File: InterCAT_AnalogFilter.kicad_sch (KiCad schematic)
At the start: 37 parts, among them T1 LM-NP-1001-B1L, T2 LM-NP-1001-B1L, T3 LM-NP-1001-B1L, T4 LM-NP-1001-B1L, U4 MCP6002, U5 MCP6002, U6 MCP6002

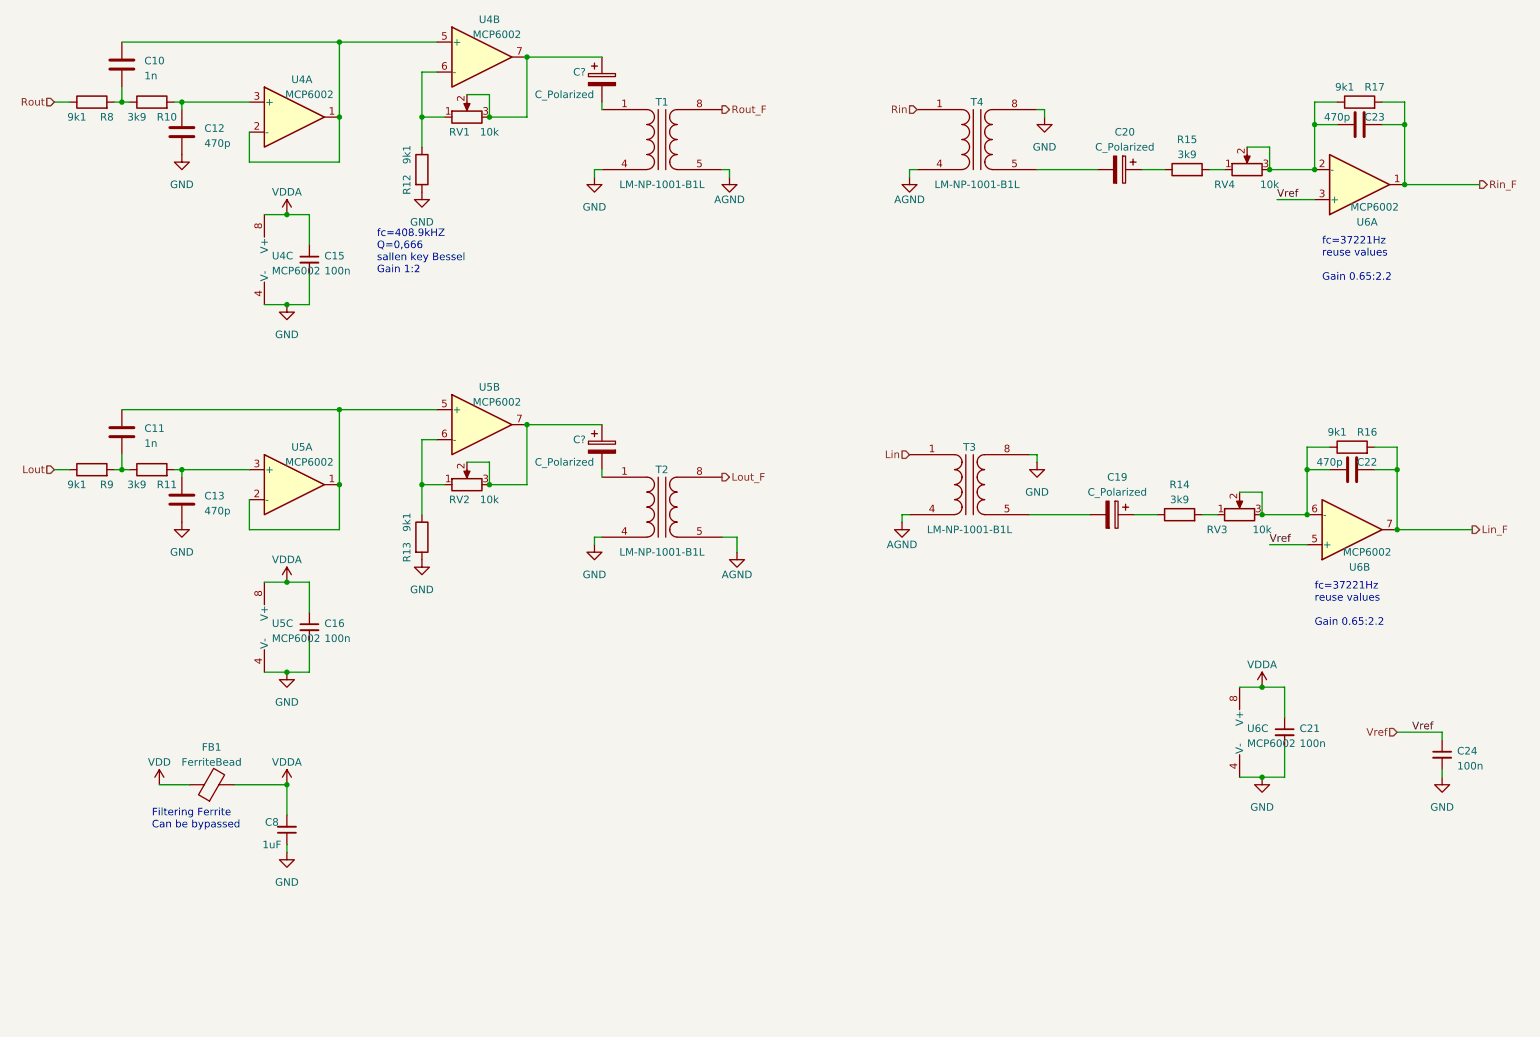
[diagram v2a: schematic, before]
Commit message: removed jack connectors, added testpoints on DAC
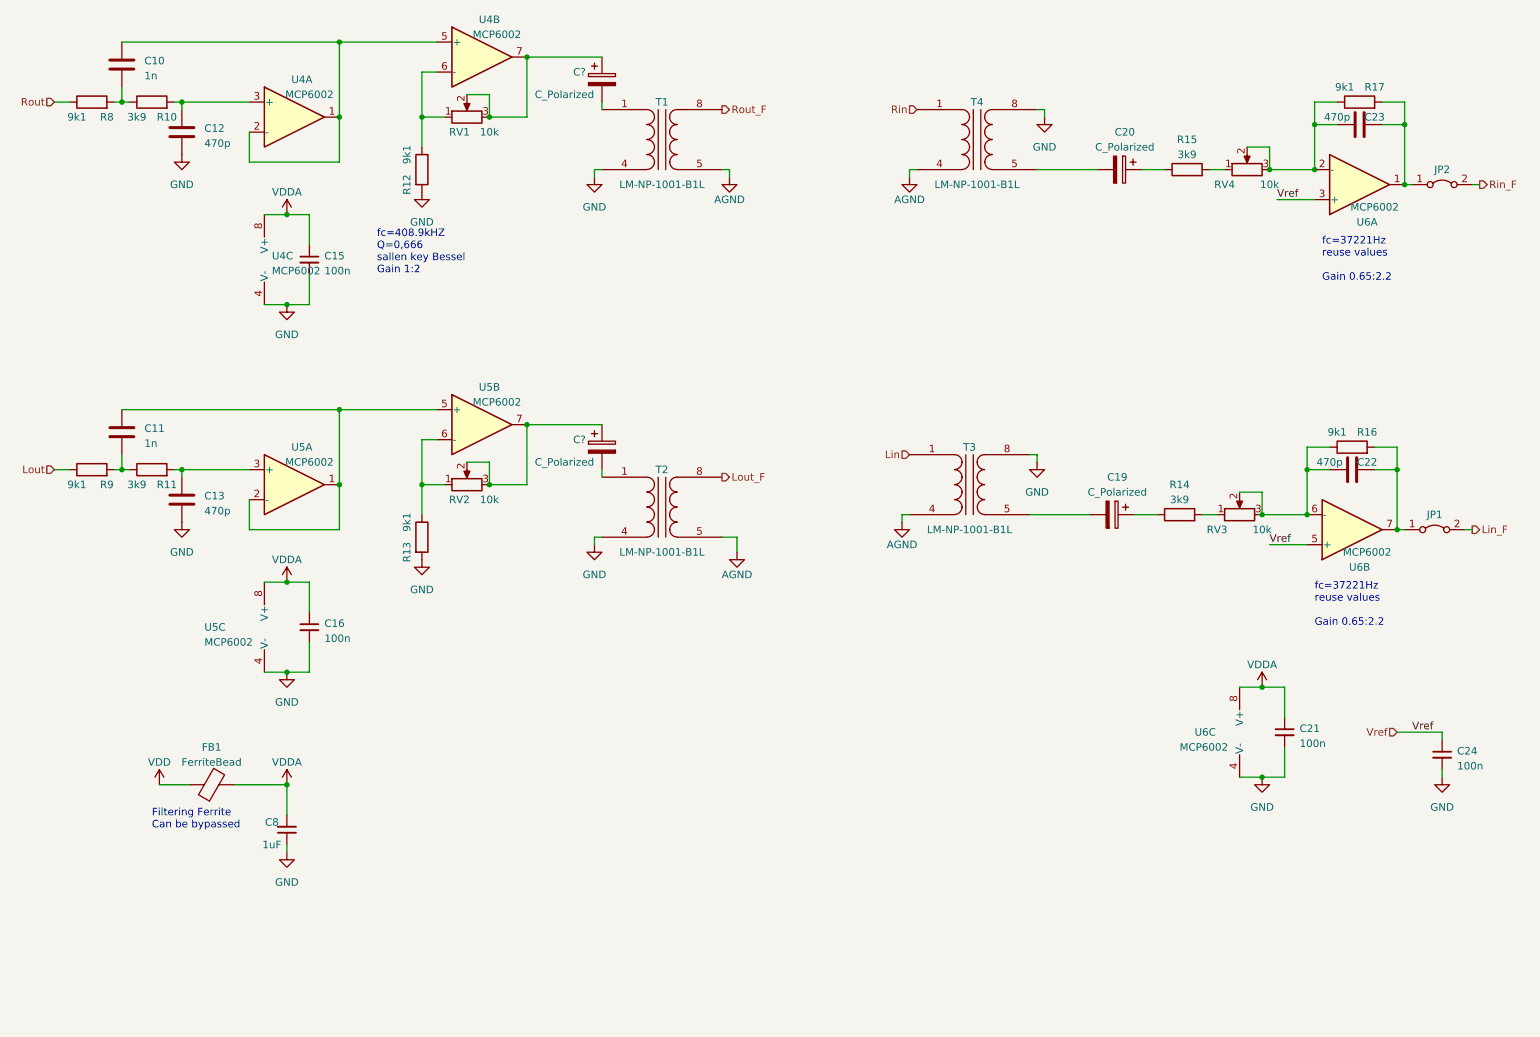
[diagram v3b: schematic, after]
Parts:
- added JP1, JP2: Jumper_2_Bridged, Jumper:SolderJumper-2_P1.3mm_Bridged_RoundedPad1.0x1.5mm, symbol Jumper:Jumper_2_Bridged
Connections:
- net Lin_F: now also JP1.2 (B); no longer C22.2, R16.2, U6.7
- net Rin_F: now also JP2.2 (B); no longer C23.2, R17.2, U6.1
- new net: C22.2, JP1.1 (A), R16.2, U6.7
- new net: C23.2, JP2.1 (A), R17.2, U6.1
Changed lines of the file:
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@@
   (junction (at 72.39 26.67) (diameter 0) (color 0 0 0 0)
   )
+  (junction (at 252.73 50.8) (diameter 0) (color 0 0 0 0)
+  )
   (junction (at 86.36 39.37) (diameter 0) (color 0 0 0 0)
   )
@@
   (junction (at 97.79 101.6) (diameter 0) (color 0 0 0 0)
   )
-  (junction (at 252.73 50.8) (diameter 0) (color 0 0 0 0)
-  )
   (junction (at 104.14 91.44) (diameter 0) (color 0 0 0 0)
   )
@@
   (junction (at 35.56 36.83) (diameter 0) (color 0 0 0 0)
   )
+  (junction (at 251.46 109.22) (diameter 0) (color 0 0 0 0)
+  )
   (junction (at 97.79 39.37) (diameter 0) (color 0 0 0 0)
   )
@@
   (junction (at 35.56 99.06) (diameter 0) (color 0 0 0 0)
   )
-  (junction (at 251.46 109.22) (diameter 0) (color 0 0 0 0)
-  )
   (junction (at 72.39 101.6) (diameter 0) (color 0 0 0 0)
   )
@@
     (stroke (width 0) (type default))
   )
+  (wire (pts (xy 264.16 50.8) (xy 265.43 50.8))
+    (stroke (width 0) (type default))
+  )
   (wire (pts (xy 236.22 99.06) (xy 240.03 99.06))
     (stroke (width 0) (type default))
@@
     (stroke (width 0) (type default))
   )
-  (wire (pts (xy 251.46 109.22) (xy 264.16 109.22))
-    (stroke (width 0) (type default))
-  )
   (wire (pts (xy 167.64 107.95) (xy 167.64 106.68))
     (stroke (width 0) (type default))
@@
     (stroke (width 0) (type default))
   )
+  (wire (pts (xy 251.46 109.22) (xy 252.73 109.22))
+    (stroke (width 0) (type default))
+  )
   (wire (pts (xy 115.57 48.26) (xy 115.57 49.53))
     (stroke (width 0) (type default))
@@
     (stroke (width 0) (type default))
   )
+  (wire (pts (xy 262.89 109.22) (xy 264.16 109.22))
+    (stroke (width 0) (type default))
+  )
   (wire (pts (xy 240.03 95.25) (xy 236.22 95.25))
     (stroke (width 0) (type default))
@@
     (stroke (width 0) (type default))
   )
+  (wire (pts (xy 252.73 50.8) (xy 254 50.8))
+    (stroke (width 0) (type default))
+  )
   (wire (pts (xy 59.69 118.11) (xy 63.5 118.11))
     (stroke (width 0) (type default))
@@
   )
   (wire (pts (xy 229.87 111.76) (xy 236.22 111.76))
-    (stroke (width 0) (type default))
-  )
-  (wire (pts (xy 252.73 50.8) (xy 265.43 50.8))
     (stroke (width 0) (type default))
   )
@@
   )
   (symbol (lib_id "Amplifier_Operational:TL082") (at 227.33 143.51 0) (unit 3)
-    (in_bom yes) (on_board yes) (dnp no) (fields_autoplaced)
-    (property "Reference" "U6" (at 226.06 142.875 0)
+    (in_bom yes) (on_board yes) (dnp no)
+    (property "Reference" "U6" (at 217.17 143.51 0)
       (effects (font (size 1.27 1.27)) (justify left))
     )
-    (property "Value" "MCP6002" (at 226.06 145.415 0)
+    (property "Value" "MCP6002" (at 214.63 146.05 0)
       (effects (font (size 1.27 1.27)) (justify left))
     )
@@
     )
   )
+  (symbol (lib_id "Jumper:Jumper_2_Bridged") (at 259.08 50.8 0) (unit 1)
+    (in_bom yes) (on_board yes) (dnp no)
+    (property "Reference" "JP2" (at 259.08 48.26 0)
+      (effects (font (size 1.27 1.27)))
+    )
+    (property "Value" "Jumper_2_Bridged" (at 259.08 48.26 0)
+      (effects (font (size 1.27 1.27)) hide)
+    )
+    (property "Footprint" "Jumper:SolderJumper-2_P1.3mm_Bridged_RoundedPad1.0x1.5mm" (at 259.08 50.8 0)
+      (effects (font (size 1.27 1.27)) hide)
+    )
+    (property "Datasheet" "~" (at 259.08 50.8 0)
+      (effects (font (size 1.27 1.27)) hide)
+    )
+    (pin "1")
+    (pin "2")
+    (instances
+      (project "Intercat"
+        (path "/03d88a85-11fd-47aa-954c-c318bb15294a/59340727-7477-481f-9a33-ca352ff8276a"
+          (reference "JP2") (unit 1)
+        )
+      )
+    )
+  )
   (symbol (lib_id "power:GND") (at 259.08 151.13 0) (unit 1)
     (in_bom yes) (on_board yes) (dnp no) (fields_autoplaced)
@@
   )
   (symbol (lib_id "Amplifier_Operational:TL082") (at 62.23 125.73 0) (unit 3)
-    (in_bom yes) (on_board yes) (dnp no) (fields_autoplaced)
-    (property "Reference" "U5" (at 60.96 125.095 0)
+    (in_bom yes) (on_board yes) (dnp no)
+    (property "Reference" "U5" (at 49.53 125.73 0)
       (effects (font (size 1.27 1.27)) (justify left))
     )
-    (property "Value" "MCP6002" (at 60.96 127.635 0)
+    (property "Value" "MCP6002" (at 49.53 128.27 0)
       (effects (font (size 1.27 1.27)) (justify left))
     )
@@
         )
       )
+    )
+  )
+  (symbol (lib_id "Jumper:Jumper_2_Bridged") (at 257.81 109.22 0) (unit 1)
+    (in_bom yes) (on_board yes) (dnp no)
+    (property "Reference" "JP1" (at 257.81 106.68 0)
+      (effects (font (size 1.27 1.27)))
+    )
+    (property "Value" "Jumper_2_Bridged" (at 257.81 106.68 0)
+      (effects (font (size 1.27 1.27)) hide)
+    )
+    (property "Footprint" "Jumper:SolderJumper-2_P1.3mm_Bridged_RoundedPad1.0x1.5mm" (at 257.81 109.22 0)
+      (effects (font (size 1.27 1.27)) hide)
+    )
+    (property "Datasheet" "~" (at 257.81 109.22 0)
+      (effects (font (size 1.27 1.27)) hide)
+    )
+    (pin "1")
+    (pin "2")
+    (instances
+      (project "Intercat"
+        (path "/03d88a85-11fd-47aa-954c-c318bb15294a/59340727-7477-481f-9a33-ca352ff8276a"
+          (reference "JP1") (unit 1)
+        )
+      )

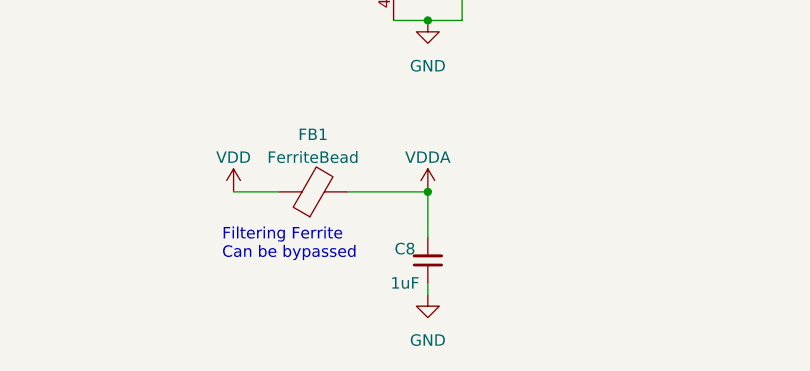
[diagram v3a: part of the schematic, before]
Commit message: changed optocouplers, started compiling BOM
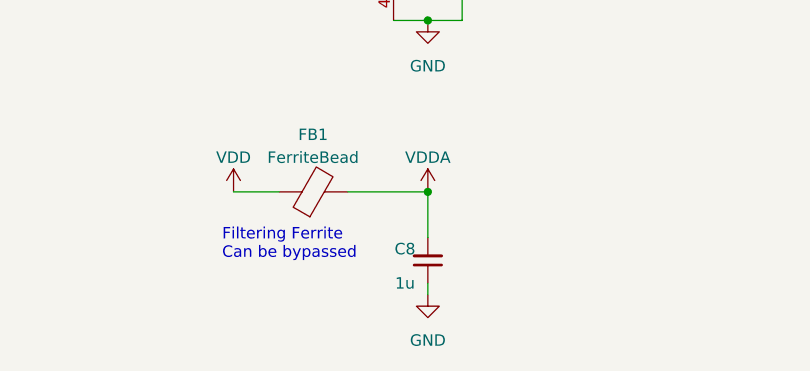
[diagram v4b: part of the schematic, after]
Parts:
- C10, C11: LCSC (none) -> C28323; Note (none) -> X7R
- C12, C13, C22, C23: LCSC (none) -> C1620; Note (none) -> X7R
- C15, C16, C21, C24: LCSC (none) -> C14663; Note (none) -> X7R
- C8: value 1uF -> 1u; footprint Capacitor_SMD:C_0603_1608Metric -> Capacitor_SMD:C_0805_2012Metric; LCSC (none) -> C28323; Note (none) -> X7R
- R10, R11, R14, R15: LCSC (none) -> C23018
- R12, R13, R16, R17, R8, R9: LCSC (none) -> C23260
- U4, U5, U6: LCSC (none) -> C7377

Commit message: continuation on BOM
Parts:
- T1, T2, T3, T4: LCSC (none) -> C5361839
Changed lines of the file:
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@@
       (effects (font (size 1.27 1.27)) hide)
     )
-    (property "LCSC" "" (at 127 43.18 0)
+    (property "LCSC" "C5361839" (at 127 43.18 0)
       (effects (font (size 1.27 1.27)) hide)
     )
@@
       (effects (font (size 1.27 1.27)) hide)
     )
-    (property "LCSC" "" (at 179.07 101.6 0)
+    (property "LCSC" "C5361839" (at 179.07 101.6 0)
       (effects (font (size 1.27 1.27)) hide)
     )
@@
       (effects (font (size 1.27 1.27)) hide)
     )
-    (property "LCSC" "" (at 180.34 43.18 0)
+    (property "LCSC" "C5361839" (at 180.34 43.18 0)
       (effects (font (size 1.27 1.27)) hide)
     )
@@
       (effects (font (size 1.27 1.27)) hide)
     )
-    (property "LCSC" "" (at 127 105.41 0)
-      (effects (font (size 1.27 1.27)) hide)
-    )
+    (property "LCSC" "C5361839" (at 127 105.41 0)
+      (effects (font (size 1.27 1.27)) hide)
+    )

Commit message: added FB2 and continued with BOM
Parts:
- FB1: LCSC (none) -> C1002; Note (none) -> 600R@100MHz
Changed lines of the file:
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@@
       (effects (font (size 1.27 1.27)) hide)
     )
-    (property "LCSC" "" (at 50.8 152.4 0)
+    (property "LCSC" "C1002" (at 50.8 152.4 0)
       (effects (font (size 1.27 1.27)) hide)
     )
-    (property "Note" "" (at 50.8 152.4 0)
+    (property "Note" "600R@100MHz" (at 50.8 152.4 0)
       (effects (font (size 1.27 1.27)) hide)
     )
